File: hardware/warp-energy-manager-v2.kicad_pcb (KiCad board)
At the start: 4 copper layers, 68 x 87 mm, 114 parts, among them J101 Boot, J102 DM3CS, P101 CON-SENSOR2, P102 SG-Ready, P103 L+N, P104 OUT, P105 INPUT, P110 MODBUS, P111 Debug, Q101 2N7002P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

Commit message: routing started
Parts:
- removed D107: B0520LW-7, kicad-libraries:SOD-123
- removed D110: blue, kicad-libraries:D0603E
- removed R103, R114: 1k, kicad-libraries:R0603F
- removed RP105: 10k, kicad-libraries:4X0603
- removed U109: HCPL2731, kicad-libraries:DIP-8
- added C123: 100nF, kicad-libraries:C0603F, F.Cu at (138.8, 61.4)
- added C133: 100nF, kicad-libraries:C0603F, F.Cu at (146.1, 68.0)
- added C134: 100nF, kicad-libraries:C0603F, F.Cu at (149.7, 68.6)
- added R115: 1k, kicad-libraries:R0805E, F.Cu at (143.7, 64.3)
- added R119: 1k, kicad-libraries:R1206E, F.Cu at (147.7, 65.0)
- added R120: 1k, kicad-libraries:R0805E, F.Cu at (145.6, 64.3)
- added R121: 1k, kicad-libraries:R0805E, F.Cu at (141.8, 64.3)
- added RP104: 10k, kicad-libraries:4X0603, F.Cu at (140.2, 78.9)
- added U104: AP22811BW5, kicad-libraries:SOT25, F.Cu at (157.4, 74.7)
- added U106: IS2805-4, kicad-libraries:SOIC16_44, F.Cu at (150.0, 74.3)
- C105: value 100uF -> 2.2uF; footprint kicad-libraries:C1210 -> kicad-libraries:C0603F
- C116: value 100uF -> 100nF; footprint kicad-libraries:C1210 -> kicad-libraries:C0603F
- C124: value 1uF -> 100nF
- D101, D105: value B0520LW-7 -> LL4148; footprint kicad-libraries:SOD-123 -> kicad-libraries:MiniMelf
- D104: value blue -> LL4148; footprint kicad-libraries:D0603E -> kicad-libraries:MiniMelf
- P104: footprint kicad-libraries:OQ_4P_5mm -> kicad-libraries:OQ_4P_5mm_230V
- Q102, Q107: value SSM6N7002KFU -> 2N7002P; footprint kicad-libraries:SOT363 -> kicad-libraries:SOT23GDS
- R101: value 1k -> 10k; footprint kicad-libraries:R1206E -> kicad-libraries:R0603F
- R102, R118: value 1k -> 10k
- R104, R105, R112, R116, R117: footprint kicad-libraries:R1206E -> kicad-libraries:R0805E
- R110, R113: footprint kicad-libraries:R0402F -> kicad-libraries:R0603F
- moved C122 149.2 mm to (137.7, 104.3), turned to 180 degrees
- moved C131 148.3 mm to (124.2, 86.9), turned to 90 degrees
- moved C127 148.3 mm to (125.5, 86.9), turned to 90 degrees
- moved R118 144.0 mm to (122.5, 77.9), turned to 180 degrees
- moved R136 143.0 mm to (145.4, 103.8), turned to 180 degrees
- moved R135 142.1 mm to (148.3, 103.8), turned to 180 degrees
- moved R134 141.4 mm to (151.2, 103.8), turned to 180 degrees
- moved Q103 131.0 mm to (122.5, 75.5), turned to 180 degrees
- moved C132 130.6 mm to (154.4, 102.4), turned to 180 degrees
- moved C120 129.7 mm to (141.4, 104.0)
- moved U113 129.5 mm to (148.6, 99.5), turned to -90 degrees
- moved RP102 126.6 mm to (124.6, 83.6), turned to 90 degrees
- moved C121 125.6 mm to (141.4, 101.8)
- moved C115 124.3 mm to (155.0, 104.3)
- moved C111 124.1 mm to (98.2, 89.3), turned to -90 degrees
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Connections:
- C104 pad 1: Net-(C104-Pad1) -> Net-(P105-P2)
- C107 pad 1: Net-(C107-Pad1) -> Net-(P105-P3)
- C115 pad 2: Net-(P110-P1) -> VCC
- C116 pad 1: Net-(C116-Pad1) -> Net-(P105-P5)
- C124 pad 1: VCC -> Net-(C124-Pad1)
- D104 pad 1: VCC -> Net-(D104-A)
- D104 pad 2: Net-(D104-K) -> VCC
- L104 pad 2: Net-(D111-A) -> Net-(D106-A)
- L104 pad 3: Net-(D106-A) -> Net-(D111-A)
- L104 pad 6: Net-(P110-P3) -> Net-(P110-P2)
- L104 pad 7: Net-(P110-P2) -> Net-(P110-P3)
- P105 pad 1: unconnected-(P105-P1-Pad1) -> Net-(P105-P1)
- P105 pad 2: unconnected-(P105-P2-Pad2) -> Net-(P105-P2)
- P105 pad 3: unconnected-(P105-P3-Pad3) -> Net-(P105-P3)
- P105 pad 4: unconnected-(P105-P4-Pad4) -> Net-(P105-P4)
- P105 pad 5: unconnected-(P105-P5-Pad5) -> Net-(P105-P5)
- P105 pad 6: unconnected-(P105-P6-Pad6) -> Net-(P105-P6)
- Q103 pad D: Net-(D107-A) -> Net-(D104-A)
- R104 pad 1: Net-(C104-Pad1) -> Net-(P105-P2)
- R105 pad 1: Net-(C107-Pad1) -> Net-(P105-P3)
- R111 pad 1: unconnected-(R111-Pad1) -> Net-(P105-P1)
- R112 pad 1: Net-(C104-Pad1) -> Net-(P105-P2)
- R116 pad 1: unconnected-(R116-Pad1) -> Net-(P105-P6)
- R116 pad 2: VCC -> GND
- R117 pad 1: Net-(C107-Pad1) -> Net-(P105-P3)
- R124 pad 1: Net-(U101B-P0.6_IO) -> Net-(U101D-P2.9_AI)
- REL101 pad 3: Net-(P102-P3) -> unconnected-(REL101-Pad3)
- REL101 pad 4: Net-(P102-P4) -> unconnected-(REL101-Pad4)
- REL101 pad 5: unconnected-(REL101-Pad5) -> Net-(P102-P4)
- REL101 pad 6: unconnected-(REL101-Pad6) -> Net-(P102-P3)
- REL101 pad 8: Net-(D107-A) -> Net-(D104-A)
- REL102 pad 3: Net-(P102-P1) -> unconnected-(REL102-Pad3)
- REL102 pad 4: Net-(P102-P2) -> unconnected-(REL102-Pad4)
- REL102 pad 5: unconnected-(REL102-Pad5) -> Net-(P102-P2)
- REL102 pad 6: unconnected-(REL102-Pad6) -> Net-(P102-P1)
- U101 pad 10: IN1 -> IN3
- U101 pad 12: unconnected-(U101D-P2.9_AI-Pad12) -> Net-(U101D-P2.9_AI)
- U101 pad 35: Net-(U101B-P0.6_IO) -> unconnected-(U101B-P0.6_IO-Pad35)
- U101 pad 6: unconnected-(U101D-P2.3_AI-Pad6) -> V12
- U101 pad 7: V12 -> IN0
- U101 pad 8: unconnected-(U101D-P2.5_AI-Pad8) -> IN1
- U101 pad 9: IN0 -> IN2
- U102 pad 1: L -> N
- U102 pad 2: N -> L
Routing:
- net VCC: track 45.8 -> 86.5 mm, vias 3 -> 11
- net Net-(L103-Pad1): track 39.4 -> 0.00 mm, vias 4 -> 0
- net SD-CDS: track 45.8 -> 9.48 mm, vias 2 -> 1
- net L: track 0.00 -> 33.7 mm
- net Net-(D105-A): track 0.00 -> 15.2 mm
- net GND: track 124.1 -> 109.0 mm, vias 86 -> 70
- net Net-(P104-P2): track 0.00 -> 14.7 mm
- net 3V3: track 27.8 -> 13.3 mm, vias 10 -> 5
- net N: track 0.00 -> 14.1 mm
- net Net-(P104-P4): track 0.00 -> 14.0 mm
- net S-MISO: track 17.8 -> 5.91 mm
- net Net-(P110-P1): track 0.00 -> 11.7 mm
- net Net-(C116-Pad1): track 11.6 -> 0.00 mm
- net Net-(P110-P2): track 0.00 -> 11.2 mm
- net Net-(J102-DAT3): track 11.2 -> 0.00 mm
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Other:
- outline, holes or cut-outs redrawn
- board text added: "230V Fuse"
- board text added: "230VAC"
- board text added: "RS485"
- board text added: "Status"
- board text removed: "Fuse Power"
- board text removed: "N"

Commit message: fix schematic drcs
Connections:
- U101 pad 25: SD-EN -> unconnected-(U101C-P1.1_IHO-Pad25)
- U101 pad 4: SD-CDS -> SD-EN
- U101 pad 5: unconnected-(U101D-P2.2_AI-Pad5) -> SD-CDS
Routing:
- net SD-CDS: track 9.48 -> 29.5 mm, vias 1 -> 2
- net S-MISO: track 5.91 -> 17.9 mm
- net SD-EN: track 0.00 -> 1.95 mm, vias 0 -> 1
- net SD-CLK: track 3.58 -> 4.20 mm
- net SD-MOSI: track 3.18 -> 3.70 mm

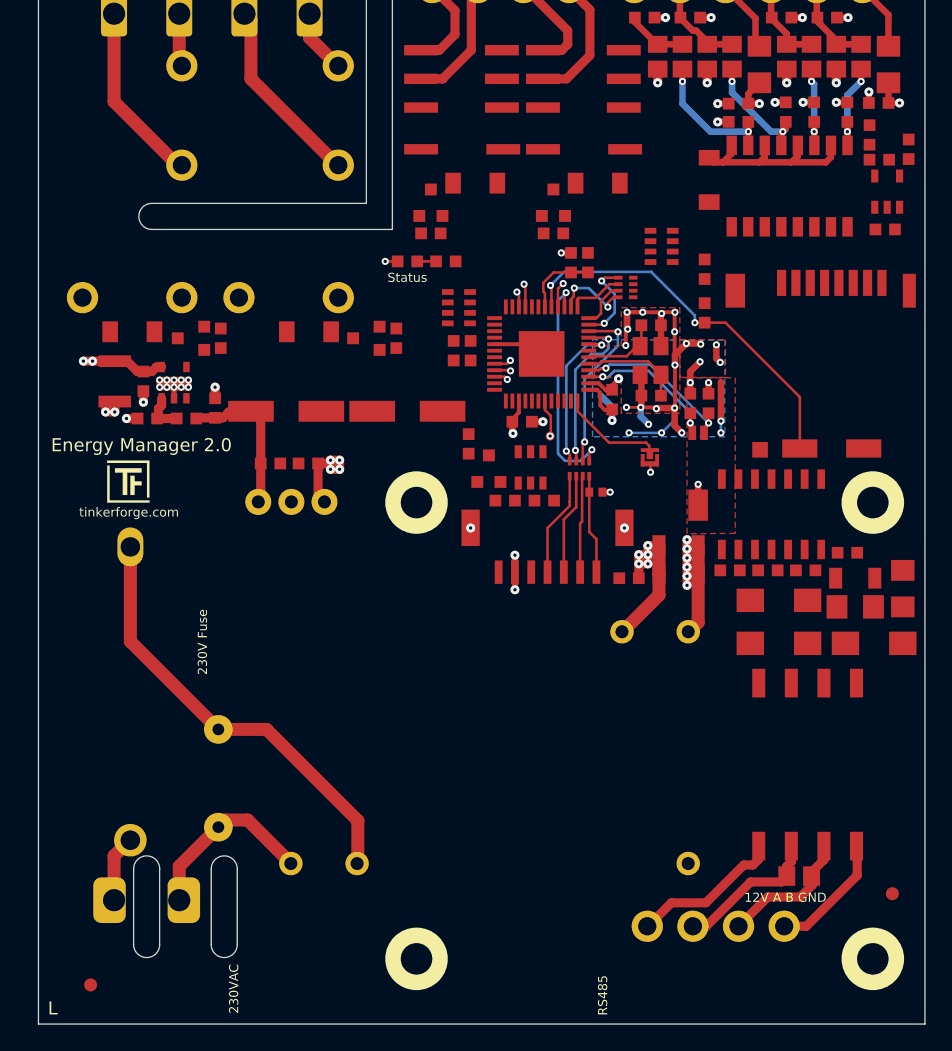
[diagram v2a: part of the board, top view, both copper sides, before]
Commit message: fully routed
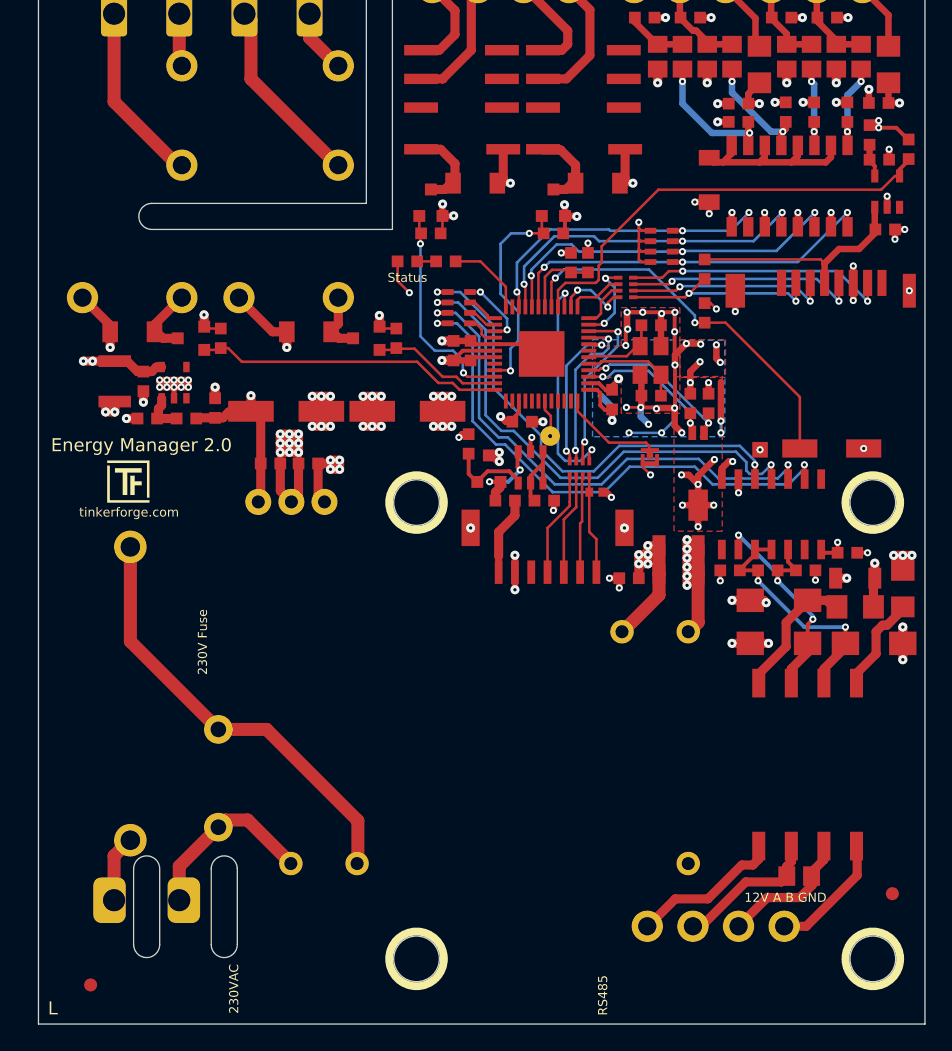
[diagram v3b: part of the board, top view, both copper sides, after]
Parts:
- C102, C117, C118, C119, C128, C129, C130: footprint C0603F -> kicad-libraries:C0603F
- L104: value WE-SL -> VAL**
- P111: footprint kicad-libraries:DEBUG_PAD -> kicad-libraries:TSTP_STL
- turned RP102 to -90 degrees
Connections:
- U101 pad 21: RELAY1 -> SG-OUT-1
- U101 pad 22: RELAY0 -> SG-OUT-0
- U101 pad 23: SG-OUT-1 -> RELAY1
- U101 pad 24: SG-OUT-0 -> RELAY0
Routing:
- net VCC: track 86.5 -> 240.7 mm, vias 11 -> 17
- net 3V3: track 13.3 -> 161.7 mm, vias 5 -> 18
- net GND: track 109.0 -> 191.2 mm, vias 70 -> 137
- net Net-(RP102-R1): track 0.00 -> 41.3 mm, vias 0 -> 2
- net Net-(RP102-R2): track 0.00 -> 39.9 mm, vias 0 -> 2
- net Net-(RP102-R3): track 0.00 -> 39.1 mm, vias 0 -> 2
- net Net-(RP102-R4): track 0.00 -> 37.0 mm, vias 0 -> 2
- net SD-EN: track 1.95 -> 34.0 mm, vias 1 -> 0
- net 5V: track 11.9 -> 42.8 mm, vias 0 -> 4
- net IN0: track 0.00 -> 30.0 mm, vias 0 -> 3
- net IN1: track 0.00 -> 28.8 mm, vias 0 -> 3
- net IN2: track 1.78 -> 26.7 mm, vias 1 -> 3
- net RELAY0: track 1.06 -> 23.7 mm, vias 1 -> 0
- net IN3: track 1.20 -> 23.7 mm, vias 1 -> 3
- net Net-(J102-DAT0): track 0.00 -> 20.5 mm, vias 0 -> 2
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- added copper zone on In1.Cu, net GND

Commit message: all bugs fixed
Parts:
- L104: value VAL** -> WE-SL
- moved P111 9.15 mm to (139.4, 98.2)
- moved J101 1.00 mm to (138.2, 95.1)
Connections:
- P111 pad 1: Net-(U101B-P0.2_IO) -> Net-(U101B-P0.6_IO)
- U101 pad 31: Net-(U101B-P0.2_IO) -> unconnected-(U101B-P0.2_IO-Pad31)
- U101 pad 35: unconnected-(U101B-P0.6_IO-Pad35) -> Net-(U101B-P0.6_IO)
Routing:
- net Net-(U101B-P0.6_IO): track 0.00 -> 10.7 mm
- net Net-(U101B-P0.2_IO): track 2.90 -> 0.00 mm, vias 1 -> 0
- net Net-(P105-P6): track 4.70 -> 7.00 mm
- net 3V3: track 161.7 -> 163.7 mm
- net IN3: track 23.7 -> 24.8 mm
- net BOOT: track 8.10 -> 7.07 mm
- added copper zone on In2.Cu, net 3V3
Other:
- outline, holes or cut-outs redrawn
